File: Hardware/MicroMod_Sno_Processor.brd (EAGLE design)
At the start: 22 x 22 mm, 37 parts, among them IC1 FT230XQ, J1 MICROMOD-2222, J2 CORTEX_JTAG_DEBUG_PTH_NS, Q1 RE1C001ZP, U2 OSC_TINY_16

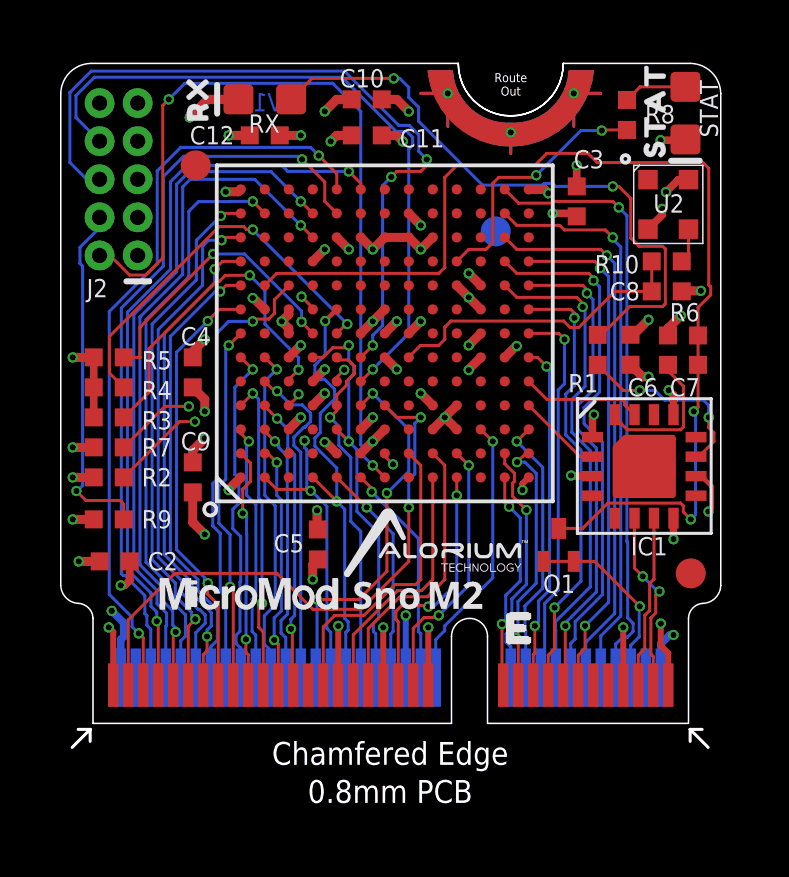
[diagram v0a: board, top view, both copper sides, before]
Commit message: V10 Update
Updated routing for DFM and proto issues
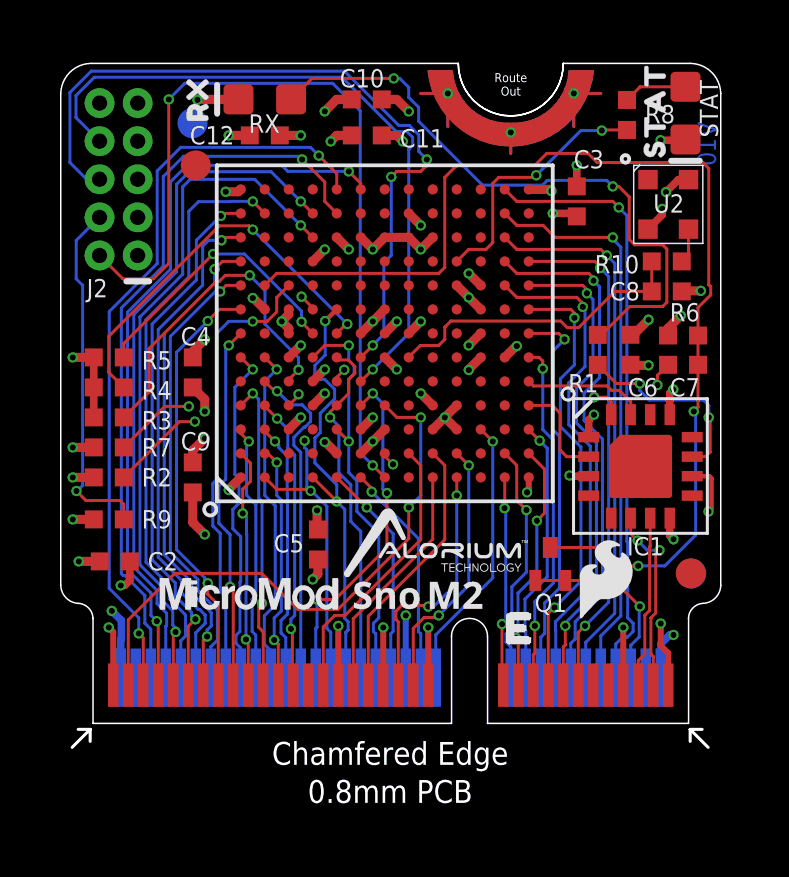
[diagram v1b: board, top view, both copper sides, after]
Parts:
- added LOGO2: SFE_LOGO_FLAME.1_INCH, SparkFun-Aesthetics:SFE_LOGO_FLAME_.1
- Q1: value RE1C001ZP -> 20V/0.1A
- R10: value 22 -> 22OHM-0402T-1/16W-1%; device New_Parts:0402-TIGHT -> SparkFun-Resistors:0402-TIGHT
- U2: value OSC_TINY_16 -> 16MHz
- moved FID3 10.7 mm to (4.39, 20.0)
- moved FID4 3.55 mm to (21.0, 5.00)
- moved Q1 0.69 mm to (16.3, 4.76)
- moved IC1 0.13 mm to (19.3, 8.57)
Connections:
- net LED renamed STAT
- removed net TXLED: IC1.5
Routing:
- net D0: track 12.6 -> 11.6 mm
- net RESET_N: track 35.7 -> 36.6 mm
- net D25: track 10.2 -> 9.44 mm
- net DTR: track 4.87 -> 4.15 mm, vias 0 -> 2
- net RX: track 2.83 -> 3.43 mm
- net D27: track 9.48 -> 8.95 mm
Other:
- board text added: "Alorium Technology"

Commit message: V10 QC changes
- Added voltage range to FPGA
- Updated RX LED to yellow
- Updated PROD_ID for 22 ohm resistor
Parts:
- R10: value 22OHM-0402T-1/16W-1% -> 22
- RX: value BLUE -> Yellow
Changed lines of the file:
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@@
 <?xml version="1.0" encoding="utf-8"?>
 <!DOCTYPE eagle SYSTEM "eagle.dtd">
-<eagle version="9.6.2">
+<eagle version="9.5.2">
 <drawing>
 <settings>
@@
 <layer number="2" name="Route2" color="1" fill="3" visible="no" active="yes"/>
 <layer number="3" name="Route3" color="4" fill="3" visible="no" active="no"/>
-<layer number="8" name="Route8" color="1" fill="2" visible="yes" active="yes"/>
-<layer number="9" name="Route9" color="4" fill="2" visible="yes" active="yes"/>
-<layer number="10" name="Route10" color="1" fill="7" visible="yes" active="yes"/>
-<layer number="11" name="Route11" color="4" fill="7" visible="yes" active="yes"/>
-<layer number="12" name="Route12" color="1" fill="5" visible="yes" active="yes"/>
-<layer number="13" name="Route13" color="4" fill="5" visible="yes" active="yes"/>
+<layer number="4" name="Route4" color="1" fill="4" visible="no" active="no"/>
+<layer number="5" name="Route5" color="4" fill="4" visible="no" active="no"/>
+<layer number="6" name="Route6" color="1" fill="8" visible="no" active="no"/>
+<layer number="7" name="Route7" color="4" fill="8" visible="no" active="no"/>
+<layer number="8" name="Route8" color="1" fill="2" visible="no" active="yes"/>
+<layer number="9" name="Route9" color="4" fill="2" visible="no" active="yes"/>
+<layer number="10" name="Route10" color="1" fill="7" visible="no" active="yes"/>
+<layer number="11" name="Route11" color="4" fill="7" visible="no" active="yes"/>
+<layer number="12" name="Route12" color="1" fill="5" visible="no" active="yes"/>
+<layer number="13" name="Route13" color="4" fill="5" visible="no" active="yes"/>
 <layer number="14" name="Route14" color="1" fill="6" visible="no" active="no"/>
-<layer number="15" name="Route15" color="4" fill="6" visible="yes" active="yes"/>
+<layer number="15" name="Route15" color="4" fill="6" visible="no" active="yes"/>
 <layer number="16" name="Bottom" color="1" fill="1" visible="yes" active="yes"/>
 <layer number="17" name="Pads" color="2" fill="1" visible="yes" active="yes"/>
@@
 <attribute name="VALUE" value="1k" x="2.235" y="8.705" size="1.27" layer="27" rot="R180"/>
 </element>
-<element name="R10" library="SparkFun-Resistors" package="0402-TIGHT" value="22OHM-0402T-1/16W-1%" x="20.2" y="15.4" smashed="yes" rot="R180">
+<element name="R10" library="SparkFun-Resistors" package="0402-TIGHT" value="22" x="20.2" y="15.4" smashed="yes" rot="R180">
 <attribute name="NAME" x="17.8" y="15" size="0.6096" layer="25"/>
-<attribute name="PROD_ID" value="RES-14340" x="20.2" y="15.4" size="1.778" layer="27" rot="R180" display="off"/>
+<attribute name="PROD_ID" value="RES-12427" x="20.2" y="15.4" size="1.778" layer="27" rot="R180" display="off"/>
+<attribute name="VALUE" value="22Ω" x="20.2" y="15.4" size="1.778" layer="27" rot="R180" display="off"/>
 </element>
 <element name="C8" library="SparkFun-Capacitors" package="0402-TIGHT" value="0.5pF" x="20.2" y="14.4" smashed="yes">
@@
 <attribute name="VALUE" value="1k" x="15.995" y="13.085" size="1.27" layer="27" rot="R270"/>
 </element>
-<element name="RX" library="SparkFun-LED" package="LED-0603" value="BLUE" x="6.8" y="20.8" smashed="yes" rot="R180">
+<element name="RX" library="SparkFun-LED" package="LED-0603" value="Yellow" x="6.8" y="20.8" smashed="yes" rot="R180">
 <attribute name="NAME" x="7.3" y="20.3" size="0.6096" layer="25" rot="R180"/>
-<attribute name="PROD_ID" value="DIO-08575" x="6.8" y="20.8" size="1.778" layer="27" rot="R180" display="off"/>
-<attribute name="VALUE" value="BLUE" x="7.8" y="22.8" size="1.27" layer="27" rot="R180"/>
+<attribute name="PROD_ID" value="DIO-09003" x="6.8" y="20.8" size="1.778" layer="27" rot="R180" display="off"/>
+<attribute name="VALUE" value="Yellow" x="7.8" y="22.8" size="1.27" layer="27" rot="R180"/>
 </element>
 <element name="FID1" library="SparkFun-Aesthetics" package="FIDUCIAL-1X2" value="FIDUCIAL1X2" x="21" y="5" smashed="yes"/>

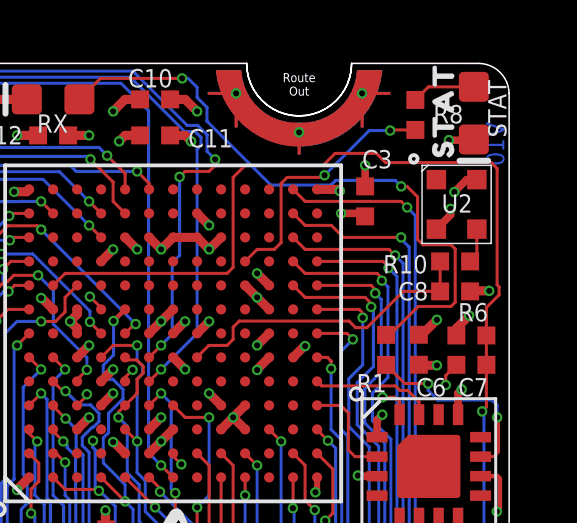
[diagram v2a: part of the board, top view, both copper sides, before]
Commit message: Updated oscillator
Updated oscillator to a smaller 2.0x1.6mm package
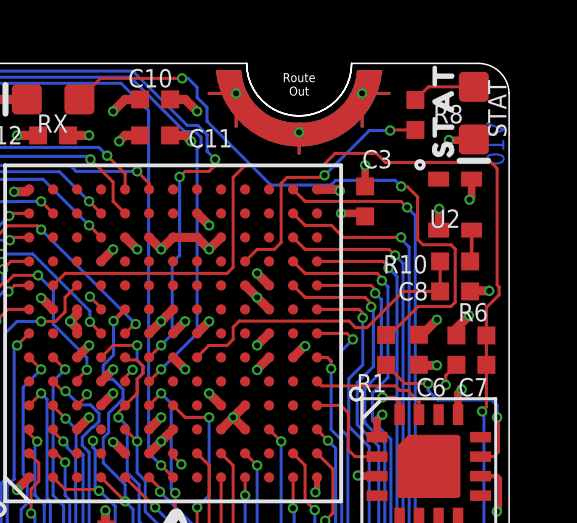
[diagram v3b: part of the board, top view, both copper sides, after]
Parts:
- U2: device New_Parts:SMD25X20 -> New_Parts:SMD20X16
- moved U2 0.65 mm to (20.2, 17.3)
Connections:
- net 3.3V: now also U2.4; no longer U2.P$4
- net GND: now also U2.2; no longer U2.P$2
- net OSC: now also U2.3; no longer U2.P$3
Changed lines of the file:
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@@
 <layer number="2" name="Route2" color="1" fill="3" visible="no" active="yes"/>
 <layer number="3" name="Route3" color="4" fill="3" visible="no" active="no"/>
-<layer number="4" name="Route4" color="1" fill="4" visible="no" active="no"/>
-<layer number="5" name="Route5" color="4" fill="4" visible="no" active="no"/>
-<layer number="6" name="Route6" color="1" fill="8" visible="no" active="no"/>
-<layer number="7" name="Route7" color="4" fill="8" visible="no" active="no"/>
+<layer number="4" name="Route4" color="18" fill="1" visible="no" active="no"/>
+<layer number="5" name="Route5" color="19" fill="1" visible="no" active="no"/>
+<layer number="6" name="Route6" color="25" fill="1" visible="no" active="no"/>
+<layer number="7" name="Route7" color="26" fill="1" visible="no" active="no"/>
 <layer number="8" name="Route8" color="1" fill="2" visible="no" active="yes"/>
 <layer number="9" name="Route9" color="4" fill="2" visible="no" active="yes"/>
@@
 <layer number="25" name="tNames" color="7" fill="1" visible="no" active="yes"/>
 <layer number="26" name="bNames" color="7" fill="1" visible="no" active="yes"/>
-<layer number="27" name="tValues" color="7" fill="1" visible="no" active="yes"/>
+<layer number="27" name="tValues" color="7" fill="1" visible="yes" active="yes"/>
 <layer number="28" name="bValues" color="7" fill="1" visible="no" active="yes"/>
 <layer number="29" name="tStop" color="7" fill="3" visible="no" active="yes"/>
@@
 </element>
 <element name="J1" library="SparkFun-MicroMod" package="M.2-CARD-E-22" value="MICROMOD-2222" x="11" y="0" smashed="yes"/>
-<element name="U2" library="New_Parts" package="SMD25X20" value="16MHz" x="20.6" y="17.8" smashed="yes" rot="R270">
-<attribute name="DIGIKEY_PART" value="535-11726-2-ND" x="20.6" y="17.8" size="1.778" layer="27" rot="R270" display="off"/>
-<attribute name="NAME" x="19.75" y="17.025" size="0.6096" layer="25"/>
-<attribute name="PROD_ID" value="XTAL-15929" x="20.6" y="17.8" size="1.778" layer="27" rot="R270" display="off"/>
-<attribute name="VALUE" value="16MHz" x="18.85" y="18.475" size="0.254" layer="27" rot="R270"/>
+<element name="U2" library="New_Parts" package="SMD20X16" value="16MHz" x="20.2" y="17.292" smashed="yes" rot="R270">
+<attribute name="NAME" x="19.35" y="16.517" size="0.6096" layer="25"/>
+<attribute name="PROD_ID" value="XTAL-16018" x="20.2" y="17.292" size="1.778" layer="27" rot="R270" display="off"/>
+<attribute name="VALUE" value="16MHz" x="18.45" y="17.967" size="0.254" layer="27" rot="R270"/>
 </element>
 <element name="IC1" library="New_Parts" package="QFN16" package3d_urn="urn:adsk.eagle:package:14017/1" value="FT230XQ" x="19.323" y="8.566" smashed="yes">
@@
 <contactref element="C11" pad="2"/>
 <contactref element="C12" pad="2"/>
-<contactref element="U2" pad="P$2"/>
+<contactref element="U2" pad="2"/>
 <contactref element="J1" pad="33"/>
 <contactref element="J1" pad="GND2"/>
@@
 <contactref element="IC1" pad="3"/>
 <contactref element="IC1" pad="13"/>
-<wire x1="19.575" y1="16.475" x2="20.05" y2="16.95" width="0.254" layer="1"/>
-<wire x1="20.05" y1="16.95" x2="20.05" y2="17.15" width="0.254" layer="1"/>
-<via x="20.05" y="17.15" extent="1-16" drill="0.2"/>
+<via x="19.669" y="17.15" extent="1-16" drill="0.2"/>
 <wire x1="20.824" y1="19.4646" x2="20.7994" y2="19.44" width="0.254" layer="1"/>
 <wire x1="20.7994" y1="19.44" x2="19.993" y2="19.44" width="0.254" layer="1"/>
@@
 <wire x1="4.5698" y1="20.8" x2="4.554" y2="20.7842" width="0.3048" layer="1"/>
 <via x="4.554" y="20.7842" extent="1-16" drill="0.2"/>
+<wire x1="19.65" y1="16.442" x2="19.65" y2="17.131" width="0.254" layer="1"/>
+<wire x1="19.65" y1="17.131" x2="19.669" y2="17.15" width="0.254" layer="1"/>
 </signal>
 <signal name="3.3V">
@@
 <contactref element="C11" pad="1"/>
 <contactref element="C12" pad="1"/>
-<contactref element="U2" pad="P$4"/>
+<contactref element="U2" pad="4"/>
 <contactref element="J1" pad="2"/>
 <contactref element="J1" pad="74"/>
@@
 <contactref element="IC1" pad="1"/>
 <contactref element="IC1" pad="8"/>
-<wire x1="20.925" y1="18.125" x2="20.587" y2="18.125" width="0.254" layer="1"/>
-<wire x1="20.587" y1="18.125" x2="20.174" y2="17.712" width="0.254" layer="1"/>
-<via x="20.174" y="17.712" extent="1-16" drill="0.2"/>
+<via x="20.682" y="17.458" extent="1-16" drill="0.2"/>
 <wire x1="17.598" y1="9.541" x2="17.598" y2="10.116" width="0.254" layer="1"/>
 <wire x1="17.598" y1="10.116" x2="17.772" y2="10.29" width="0.254" layer="1"/>
@@
 <wire x1="12" y1="15.8" x2="12.4" y2="16.2" width="0.3048" layer="1"/>
 <wire x1="12" y1="15.8" x2="11.6" y2="16.2" width="0.3048" layer="1"/>
+<wire x1="20.75" y1="18.142" x2="20.75" y2="17.526" width="0.254" layer="1"/>
+<wire x1="20.75" y1="17.526" x2="20.682" y2="17.458" width="0.254" layer="1"/>
 </signal>
 <signal name="RESET_N">
@@
 <signal name="OSC">
 <contactref element="R10" pad="1"/>
-<contactref element="U2" pad="P$3"/>
-<wire x1="20.925" y1="16.475" x2="20.925" y2="15.625" width="0.1016" layer="1"/>
-<wire x1="20.925" y1="15.625" x2="20.7" y2="15.4" width="0.1016" layer="1"/>
+<contactref element="U2" pad="3"/>
+<wire x1="20.75" y1="16.442" x2="20.75" y2="15.45" width="0.127" layer="1"/>
+<wire x1="20.75" y1="15.45" x2="20.7" y2="15.4" width="0.127" layer="1"/>
 </signal>
 <signal name="EXT_RESET">
